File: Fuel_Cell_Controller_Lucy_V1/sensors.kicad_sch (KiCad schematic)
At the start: 12 parts, among them U7 SHT31-DIS, U9 MCP602-E/SN

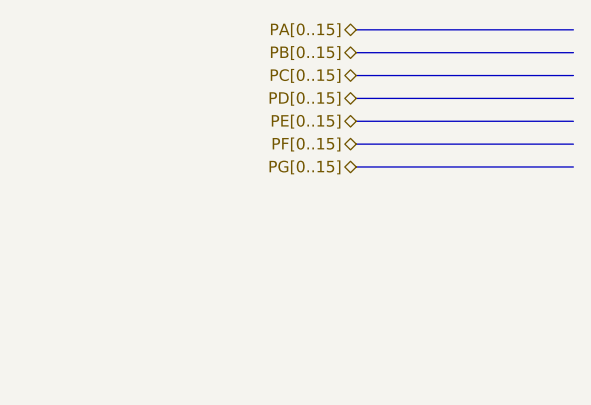
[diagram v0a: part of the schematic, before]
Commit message: Making some layout changes, added solenoid controls with opto and bjt, changed MCU
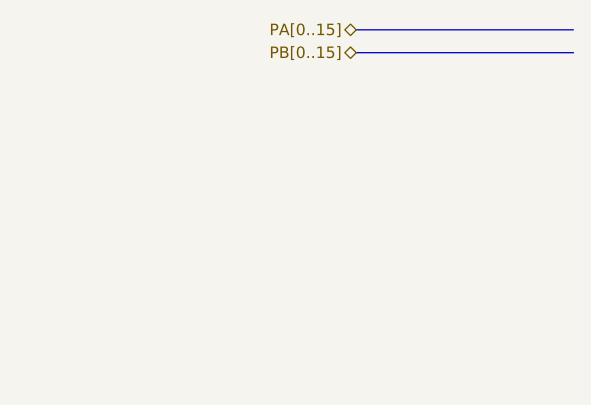
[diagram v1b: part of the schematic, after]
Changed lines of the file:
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@@
-    (stroke (width 0) (type default))
-  )
-  (bus (pts (xy 256.54 26.67) (xy 280.67 26.67))
     (stroke (width 0) (type default))
   )
@@
   )
   (wire (pts (xy 267.97 146.05) (xy 267.97 143.51))
-    (stroke (width 0) (type default))
-  )
-  (bus (pts (xy 256.54 24.13) (xy 280.67 24.13))
     (stroke (width 0) (type default))
   )
@@
     (stroke (width 0) (type default))
   )
-  (bus (pts (xy 256.54 29.21) (xy 280.67 29.21))
-    (stroke (width 0) (type default))
-  )
   (wire (pts (xy 227.33 132.08) (xy 227.33 133.35))
     (stroke (width 0) (type default))
@@
   )
   (polyline (pts (xy 96.52 76.2) (xy 96.52 27.94))
-    (stroke (width 0) (type default))
-  )
-  (bus (pts (xy 256.54 31.75) (xy 280.67 31.75))
     (stroke (width 0) (type default))
   )
@@
   )
   (wire (pts (xy 236.22 124.46) (xy 236.22 138.43))
-    (stroke (width 0) (type default))
-  )
-  (bus (pts (xy 256.54 34.29) (xy 280.67 34.29))
     (stroke (width 0) (type default))
   )
@@
     (effects (font (size 1.27 1.27)) (justify right))
   )
-  (hierarchical_label "PG[0..15]" (shape bidirectional) (at 256.54 34.29 180) (fields_autoplaced)
-    (effects (font (size 1.27 1.27)) (justify right))
-  )
-  (hierarchical_label "PE[0..15]" (shape bidirectional) (at 256.54 29.21 180) (fields_autoplaced)
-    (effects (font (size 1.27 1.27)) (justify right))
-  )
-  (hierarchical_label "PF[0..15]" (shape bidirectional) (at 256.54 31.75 180) (fields_autoplaced)
-    (effects (font (size 1.27 1.27)) (justify right))
-  )
-  (hierarchical_label "PD[0..15]" (shape bidirectional) (at 256.54 26.67 180) (fields_autoplaced)
-    (effects (font (size 1.27 1.27)) (justify right))
-  )
-  (hierarchical_label "PC[0..15]" (shape bidirectional) (at 256.54 24.13 180) (fields_autoplaced)
-    (effects (font (size 1.27 1.27)) (justify right))
-  )

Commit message: so much, can't explain
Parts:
- removed C39: 10uF, symbol Device:C
- removed D7, D8: BZV55B3V6, Diode_SMD:D_MiniMELF, symbol Diode:BZV55B3V6
- removed R27 (x3): 10k, symbol Device:R
- removed U7: SHT31-DIS, Sensor_Humidity:Sensirion_DFN-8-1EP_2.5x2.5mm_P0.5mm_EP1.1x1.7mm, symbol Sensor_Humidity:SHT31-DIS
- added C8: 100n, symbol Device:C_Small
- added D11 (x2): MMSZ5226B-7-F, FC.FTP:D_SOD_123_M, symbol FCC_Parts:MMSZ5226B-7-F
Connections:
- net +5V: now also C8.2
- net 12V_Ref: now also D11.1
- net 5V_Ref: now also D11.1
- net GND: now also C8.1, D11.2, D11.2
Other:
- note removed: "Adafruit SHT31D"
- moved on the sheet: R25, R26, R27, R28, U9A, U9B, U9C

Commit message: more things
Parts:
- removed R26: 100k, symbol Device:R
- added R25: 100k, symbol Device:R
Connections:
- net GND: now also R25.2
- net at R25.2, U9.5 (+): now also R25.1
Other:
- moved on the sheet: C8, U9C

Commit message: Again too much to say
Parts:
- added C8 (x2): 100n, Capacitor_SMD:C_0603_1608Metric, symbol Device:C_Small
- added U15, U16: ADS1115IRUGR, FC.FTP:IC_ADS1115IRUGR, symbol FCC_Parts:ADS1115IRUGR
- C8: footprint (none) -> Capacitor_SMD:C_0603_1608Metric
- R25, R27, R28: footprint (none) -> Resistor_SMD:R_0603_1608Metric
- renumbered U9 to U14
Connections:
- net +5V: now also C8.2, C8.2, U15.1 (ADDR), U15.8 (VDD), U16.8 (VDD)
- net GND: now also C8.1, C8.1, U15.3 (GND), U16.1 (ADDR), U16.3 (GND)
- net 12V_Ref renamed 12V_{REF}
- net 12V_{REF}: now also U15.5 (AIN1)
- net 5V_Ref renamed 5V_{REF}
- net 5V_{REF}: now also U15.4 (AIN0)
- new net FC_{TEMP}: U16.5 (AIN1)
- new net H2_{PRS}: U16.4 (AIN0)
- new net I2C_{SCL}: U15.10 (SCL), U16.10 (SCL)
- new net I2C_{SDA}: U15.9 (SDA), U16.9 (SDA)
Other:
- note added: "ADC's"
- note added: "I2C Addr: 0x48"
- note added: "I2C Addr: 0x49"

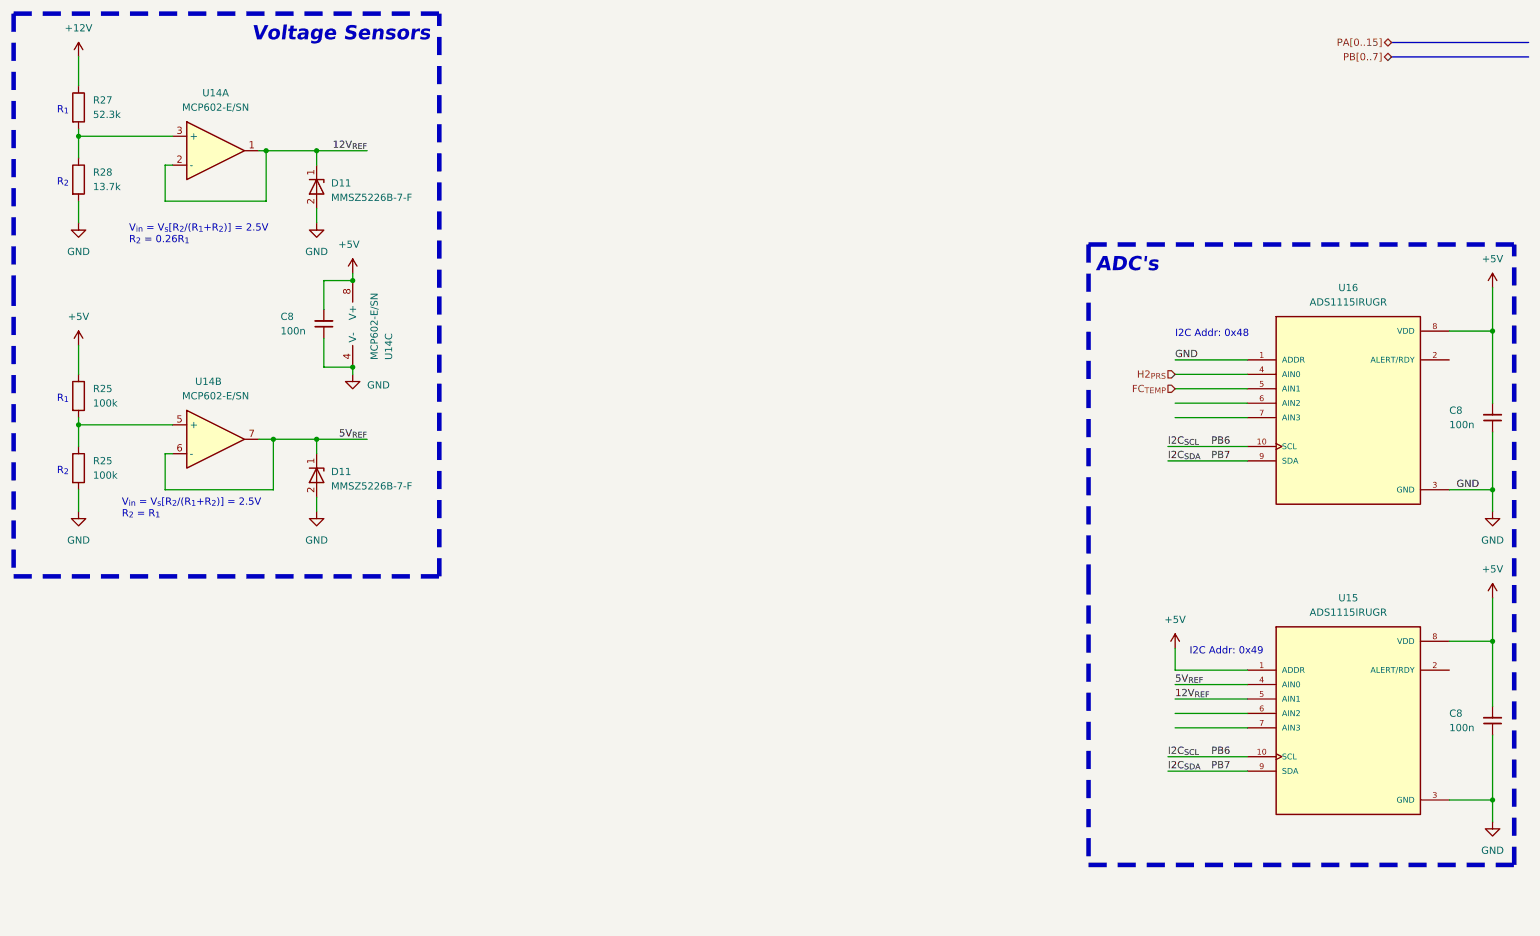
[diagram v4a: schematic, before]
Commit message: Most of the schematic done, pcb layout needs DRC
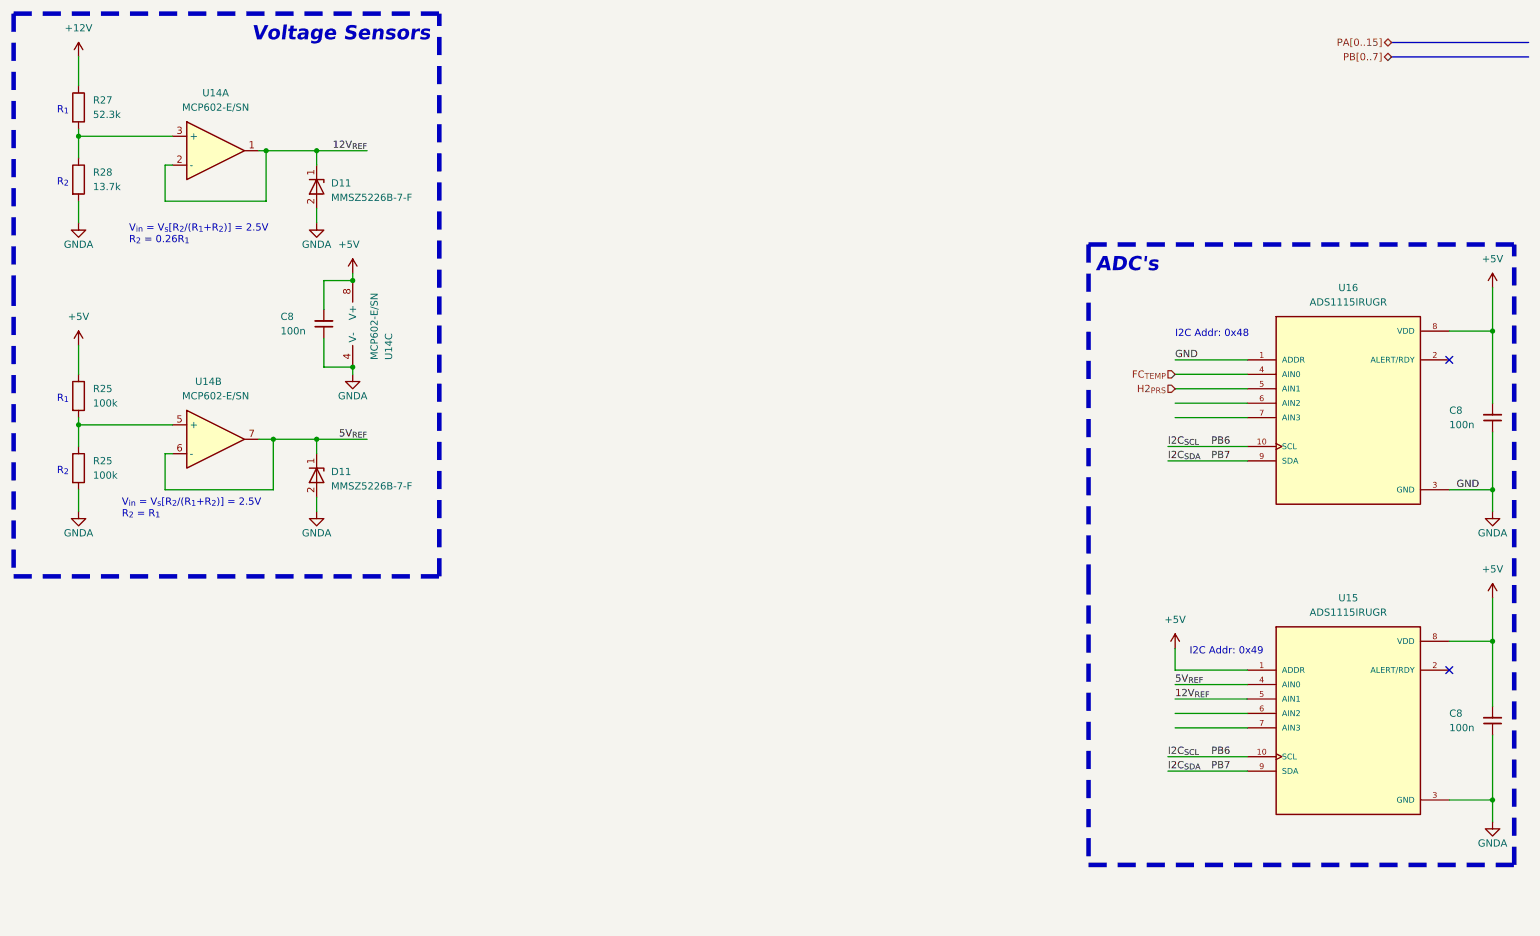
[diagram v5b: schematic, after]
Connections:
- net FC_{TEMP}: now also U16.4 (AIN0); no longer U16.5 (AIN1)
- net H2_{PRS}: now also U16.5 (AIN1); no longer U16.4 (AIN0)
- net GND renamed GNDA
- no-connect marks 0 -> 2

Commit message: So much again
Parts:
- added C35: 10u, Capacitor_SMD:CP_Elec_3x5.3, symbol Device:C_Polarized_Small
- added C8: 100n, Capacitor_SMD:C_0603_1608Metric, symbol Device:C_Small
- added U18: LIS3DHTR, FC.FTP:XDCR_LIS3DHTR, symbol FCC_Parts:LIS3DHTR
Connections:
- net GNDA: now also C35.2, C8.1, U18.10 (RES), U18.12 (GND__1), U18.5 (GND)
- net I2C_{SCL}: now also U18.4 (SCL/SPC)
- net I2C_{SDA}: now also U18.6 (SDA/SDI/SDO)
- new net +3V3: C35.1, C8.2, U18.1 (VDD_IO), U18.14 (VDD), U18.7 (SDO/SA0), U18.8 (CS)
- new net AccINT_{1}: U18.11 (INT1)
- new net AccINT_{2}: U18.9 (INT2)
- no-connect marks 2 -> 9
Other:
- note added: "Accelerometer"
- note added: "I2C Addr: 0x19"
- moved on the sheet: C8, U16

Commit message: updated
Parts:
- C8: Part# (none) -> C88219
- R25: value 100k -> 13.7k; Part# (none) -> C325658
- R27: Part# (none) -> C304764
- R28: Part# (none) -> C325658
- U14: Part# (none) -> MCP602-E/SN-ND
- U15, U16: Part# (none) -> C2651328
- U18: Part# (none) -> 497-10613-1-ND
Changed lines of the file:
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@@
+      (effects (font (size 1.27 1.27)) hide)
+    )
+    (property "Part#" "C88219" (at 274.32 95.25 0)
       (effects (font (size 1.27 1.27)) hide)
     )
@@
     )
     (property "Datasheet" "https://www.ti.com/general/docs/suppproductinfo.tsp?distId=10&gotoUrl=https%3A%2F%2Fwww.ti.com%2Flit%2Fgpn%2Fads1113" (at 248.92 95.25 0)
+      (effects (font (size 1.27 1.27)) hide)
+    )
+    (property "Part#" "C2651328" (at 248.92 95.25 0)
       (effects (font (size 1.27 1.27)) hide)
     )
@@
       (effects (font (size 1.27 1.27)) (justify left))
     )
-    (property "Value" "100k" (at 27.94 82.55 0)
+    (property "Value" "13.7k" (at 27.94 82.55 0)
       (effects (font (size 1.27 1.27)) (justify left))
     )
@@
     )
     (property "Datasheet" "~" (at 25.4 81.28 0)
+      (effects (font (size 1.27 1.27)) hide)
+    )
+    (property "Part#" "C325658" (at 25.4 81.28 0)
       (effects (font (size 1.27 1.27)) hide)
     )
@@
     )
     (property "Datasheet" "https://www.st.com/content/ccc/resource/technical/document/datasheet/3c/ae/50/85/d6/b1/46/fe/CD00274221.pdf/files/CD00274221.pdf/jcr:content/translations/en.CD00274221.pdf" (at 59.69 146.05 0)
+      (effects (font (size 1.27 1.27)) hide)
+    )
+    (property "Part#" "497-10613-1-ND" (at 59.69 146.05 0)
       (effects (font (size 1.27 1.27)) hide)
     )
@@
       (effects (font (size 1.27 1.27)) hide)
     )
+    (property "Part#" "C88219" (at 274.32 138.43 0)
+      (effects (font (size 1.27 1.27)) hide)
+    )
     (pin "1")
     (pin "2")
@@
       (effects (font (size 1.27 1.27)) hide)
     )
+    (property "Part#" "C88219" (at 88.9 135.89 0)
+      (effects (font (size 1.27 1.27)) hide)
+    )
     (pin "1")
     (pin "2")
@@
     )
     (property "Price/unit" "" (at 68.58 68.58 0)
+      (effects (font (size 1.27 1.27)) hide)
+    )
+    (property "Part#" "C88219" (at 68.58 68.58 0)
       (effects (font (size 1.27 1.27)) hide)
     )
@@
     )
     (property "Datasheet" "https://ww1.microchip.com/downloads/en/DeviceDoc/21314g.pdf" (at 49.53 38.1 0)
+      (effects (font (size 1.27 1.27)) hide)
+    )
+    (property "Part#" "MCP602-E/SN-ND" (at 49.53 38.1 0)
       (effects (font (size 1.27 1.27)) hide)
     )
@@
     )
     (property "Datasheet" "https://www.ti.com/general/docs/suppproductinfo.tsp?distId=10&gotoUrl=https%3A%2F%2Fwww.ti.com%2Flit%2Fgpn%2Fads1113" (at 248.92 139.7 0)
+      (effects (font (size 1.27 1.27)) hide)
+    )
+    (property "Part#" "C2651328" (at 248.92 139.7 0)
       (effects (font (size 1.27 1.27)) hide)
     )
@@
       (effects (font (size 1.27 1.27)) hide)
     )
+    (property "Part#" "C304764" (at 25.4 30.48 0)
+      (effects (font (size 1.27 1.27)) hide)
+    )
     (pin "1")
     (pin "2")
@@
       (effects (font (size 1.27 1.27)) (justify left))
     )
-    (property "Value" "100k" (at 27.94 95.25 0)
+    (property "Value" "13.7k" (at 27.94 95.25 0)
       (effects (font (size 1.27 1.27)) (justify left))
     )
@@
     )
     (property "Datasheet" "~" (at 25.4 93.98 0)
+      (effects (font (size 1.27 1.27)) hide)
+    )
+    (property "Part#" "C325658" (at 25.4 93.98 0)
       (effects (font (size 1.27 1.27)) hide)
     )
@@
     )
     (property "Datasheet" "https://ww1.microchip.com/downloads/en/DeviceDoc/21314g.pdf" (at 76.2 68.58 0)
+      (effects (font (size 1.27 1.27)) hide)
+    )
+    (property "Part#" "MCP602-E/SN-ND" (at 76.2 68.58 0)
       (effects (font (size 1.27 1.27)) hide)
     )
@@
       (effects (font (size 1.27 1.27)) hide)
     )
+    (property "Part#" "C325658" (at 25.4 43.18 0)
+      (effects (font (size 1.27 1.27)) hide)
+    )
     (pin "1")
     (pin "2")
@@
       (effects (font (size 1.27 1.27)) hide)
     )
+    (property "Part#" "MCP602-E/SN-ND" (at 49.53 88.9 0)
+      (effects (font (size 1.27 1.27)) hide)
+    )

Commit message: $
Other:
- note added: "Arduino -> rewrite the functions to be ported mbed Mbed - ported for Mbed Mbed api abstracts HAL layer which interacts the pins of the STM32 Chips Zypher"
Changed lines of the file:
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@@
+    (effects (font (size 1.27 1.27)) (justify left bottom))
+  )
+  (text "Arduino -> rewrite the functions to be ported mbed\nMbed - ported for Mbed Mbed api abstracts HAL layer which interacts the pins of the STM32 Chips\nZypher\n"
+    (at 97.79 92.71 0)
     (effects (font (size 1.27 1.27)) (justify left bottom))
   )
